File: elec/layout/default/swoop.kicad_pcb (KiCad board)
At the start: 2 copper layers, 100 x 100 mm, 67 parts

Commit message: ios cleanup
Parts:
- added U13: , lib:KEY-SMD_4P-L4.2-W3.2-P2.20-LS4.6, F.Cu at (113.2, 80.2)
- added U14: , lib:KEY-SMD_4P-L4.2-W3.2-P2.20-LS4.6, F.Cu at (121.4, 73.9)
- added U15: , lib:KEY-SMD_4P-L4.2-W3.2-P2.20-LS4.6, F.Cu at (113.2, 73.9)
- added U16: , lib:KEY-SMD_4P-L4.2-W3.2-P2.20-LS4.6, F.Cu at (121.4, 80.2)
- moved C11 10.2 mm to (175.0, 104.6)
- moved C12 10.2 mm to (176.1, 104.6)
- moved C13 10.2 mm to (173.7, 122.8)
- moved C3 10.2 mm to (174.0, 104.6)
- moved C4 10.2 mm to (178.0, 94.8)
- moved C8 10.2 mm to (176.4, 85.6)
- moved C9 10.2 mm to (172.6, 92.4)
- moved R10 10.2 mm to (142.4, 73.6)
- moved R13 10.2 mm to (146.8, 101.0)
- moved R7 10.2 mm to (170.7, 126.1)
- moved U1 10.2 mm to (172.7, 97.6)
- moved U2 10.2 mm to (171.3, 105.8)
- moved U9 10.2 mm to (138.3, 100.8)
- moved C15 10.2 mm to (143.7, 67.9)
- moved C16 10.2 mm to (143.6, 65.8)
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
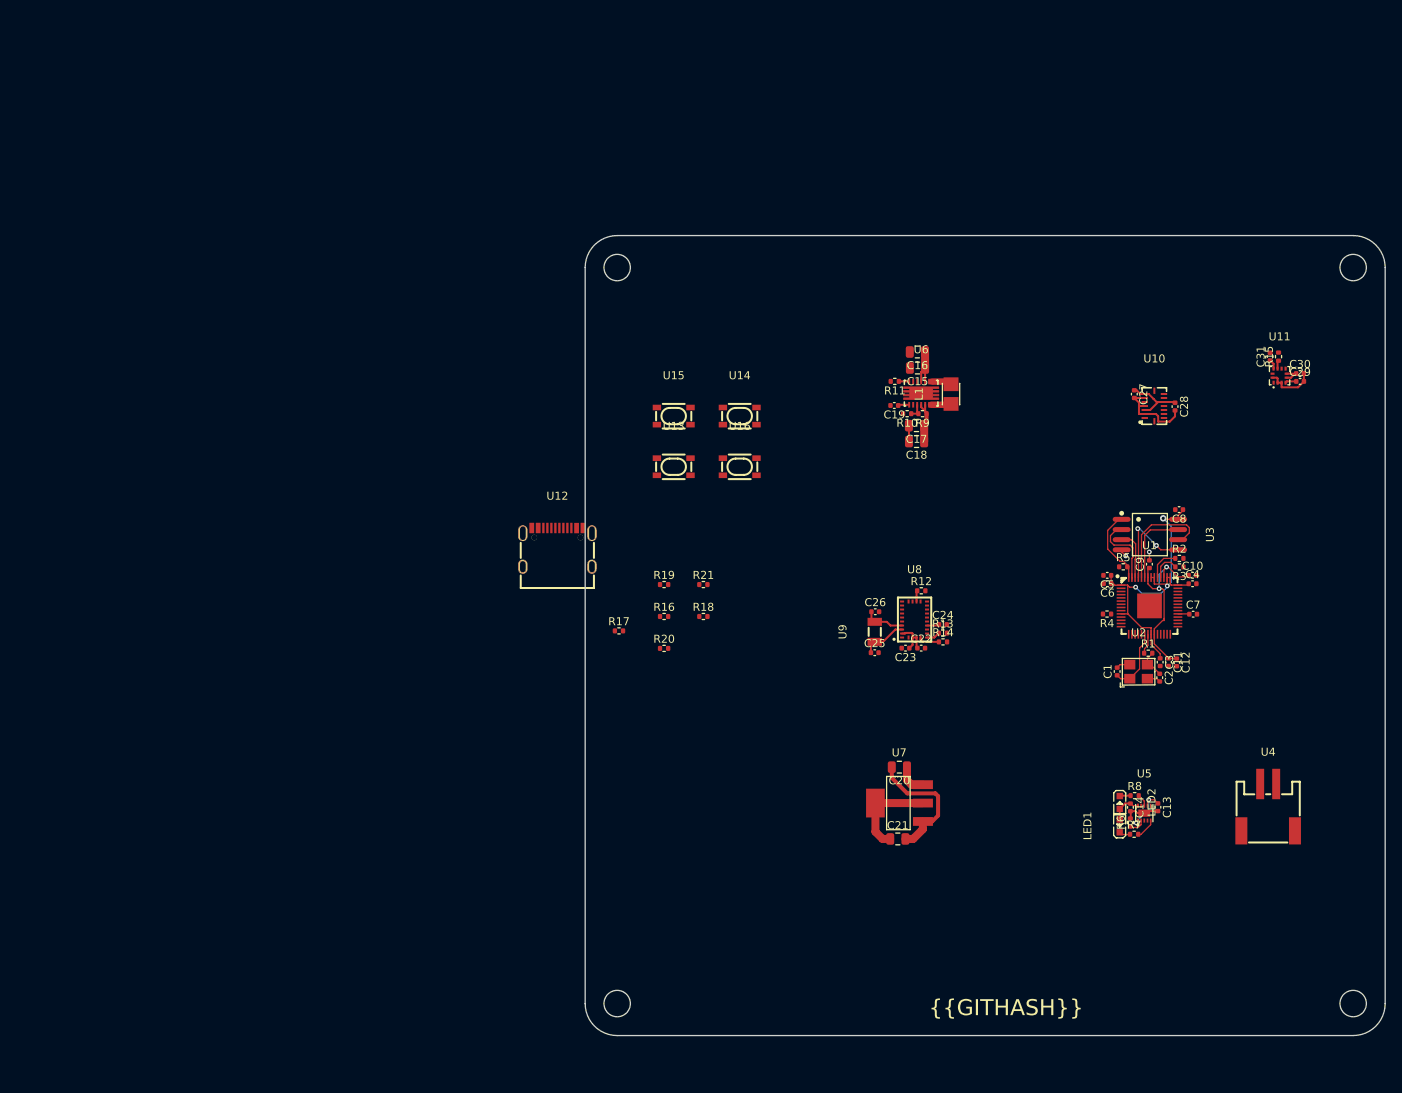
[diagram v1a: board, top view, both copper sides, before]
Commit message: layout 80% complete
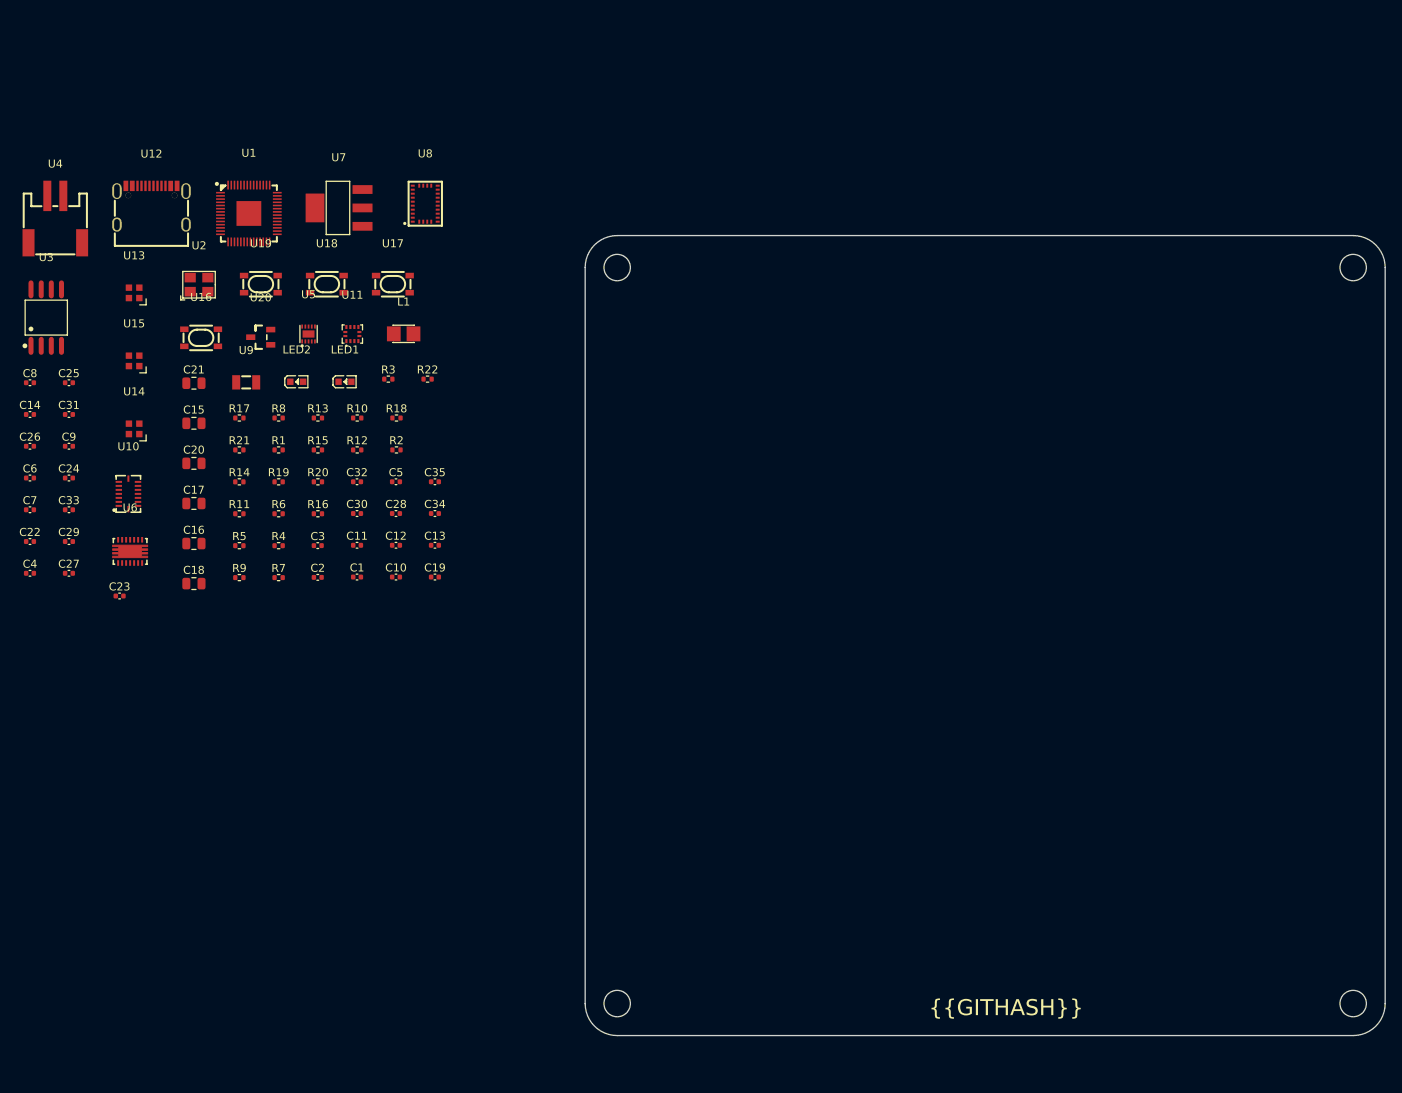
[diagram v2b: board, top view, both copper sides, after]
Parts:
- added C32: 16V 100nF X7R ±10% 0402 Multilayer Ceramic Capacitors MLCC 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, lib:C0402, F.Cu at (73.6, 82.1)
- added C33: 16V 100nF X7R ±10% 0402 Multilayer Ceramic Capacitors MLCC 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, lib:C0402, F.Cu at (37.6, 85.6)
- added C34: 16V 100nF X7R ±10% 0402 Multilayer Ceramic Capacitors MLCC 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, lib:C0402, F.Cu at (83.3, 86.0)
- added C35: 16V 100nF X7R ±10% 0402 Multilayer Ceramic Capacitors MLCC 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, lib:C0402, F.Cu at (83.3, 82.1)
- added R22: 62.5mW Thick Film Resistors ±100ppm/℃ ±1% 1kΩ 0402 Chip Res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, lib:R0402, F.Cu at (82.4, 69.2)
- added U17: , lib:KEY-SMD_4P-L4.2-W3.2-P2.20-LS4.6, F.Cu at (78.1, 57.4)
- added U18: , lib:KEY-SMD_4P-L4.2-W3.2-P2.20-LS4.6, F.Cu at (69.8, 57.4)
- added U19: , lib:KEY-SMD_4P-L4.2-W3.2-P2.20-LS4.6, F.Cu at (61.6, 57.4)
- added U20: , lib:SOT-23-3_L2.9-W1.3-P1.90-LS2.4-BR-CW, F.Cu at (61.6, 64.0)
- C13, C14: value Multilayer Ceramic Capacitors MLCC - SMD/SMT 1uF 6.3V 0402 RoHS -> 25V 1uF X5R ±10% 0402 Multilayer Ceramic Capacitors MLCC - SMD/SMT ROHS
- C15, C16, C17, C18, C20, C21: value Multilayer Ceramic Capacitors MLCC - SMD/SMT 10uF 10V 0805 RoHS -> 25V 10uF X5R ±10% 0805 Multilayer Ceramic Capacitors MLCC - SMD/SMT ROHS
- C19: value Multilayer Ceramic Capacitors MLCC - SMD/SMT 100nF 10V 0402 RoHS -> 16V 100nF X7R ±10% 0402 Multilayer Ceramic Capacitors MLCC - SMD/SMT ROHS
- R10: value Chip Resistor - Surface Mount 180KOhms ±5% 1/16W 0402 RoHS -> 62.5mW Thick Film Resistors ±100ppm/℃ ±1% 180kΩ 0402 Chip Resistor - Surface Mount ROHS
- R11, R9: value Chip Resistor - Surface Mount 1MOhms ±5% 1/16W 0402 RoHS -> 62.5mW Thick Film Resistors ±100ppm/℃ ±1% 1MΩ 0402 Chip Resistor - Surface Mount ROHS
- R7: value Chip Resistor - Surface Mount 120Ohms ±5% 1/16W 0402 RoHS -> 62.5mW Thin Film Resistor ±0.5% ±25ppm/℃ 110Ω 0402 Chip Resistor - Surface Mount ROHS
- R8: value Chip Resistor - Surface Mount 82Ohms ±5% 1/16W 0402 RoHS -> 62.5mW Thick Film Resistors ±100ppm/℃ ±1% 82Ω 0402 Chip Resistor - Surface Mount ROHS
- U13, U14, U15: footprint lib:KEY-SMD_4P-L4.2-W3.2-P2.20-LS4.6 -> lib:LED-SMD_4P-L2.0-W2.0-BR
- moved U4 168.5 mm to (35.9, 49.3)
- moved C29 155.2 mm to (37.6, 89.5)
- moved C31 150.3 mm to (37.6, 73.7), turned to 0 degrees
- moved C14 146.1 mm to (32.7, 73.7), turned to 0 degrees
- moved C7 146.0 mm to (32.7, 85.6)
- moved C4 145.3 mm to (32.7, 93.5)
- moved C8 144.5 mm to (32.7, 69.7), turned to 0 degrees
- moved U3 140.6 mm to (34.8, 61.5), turned to 0 degrees
- moved C9 135.9 mm to (37.6, 77.6), turned to 0 degrees
- moved C6 135.3 mm to (32.7, 81.6), turned to 0 degrees
- moved C27 135.0 mm to (37.6, 93.5), turned to 0 degrees
- moved U10 128.7 mm to (45.0, 83.6)
- moved U2 127.0 mm to (53.9, 57.4)
- moved U1 122.8 mm to (60.1, 48.5)
- moved R15 120.6 mm to (68.7, 78.1), turned to 0 degrees
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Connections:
- net vcc-8 renamed vcc-18
- C10 pad 1: vcc-1 -> vcc-5
- C11 pad 1: vcc-1 -> vcc-5
- C12 pad 1: vcc-1 -> vcc-5
- C13 pad 1: vcc-2 -> vcc-6
- C14 pad 1: vcc-3 -> vcc-7
- C15 pad 1: vcc-3 -> vcc-7
- C16 pad 1: vcc-3 -> vcc-7
- C17 pad 1: vcc-4 -> vcc-10
- C18 pad 1: vcc-4 -> vcc-10
- C20 pad 1: vcc-4 -> vcc-10
- C9 pad 1: vcc-1 -> vcc-5
- LED1 pad 2: vcc-3 -> vcc-7
- LED2 pad 2: vcc-3 -> vcc-7
- R18 pad 1: vcc-5 -> vcc-15
- R18 pad 2: out-2 -> vcc-2
- R19 pad 1: vcc-6 -> vcc-16
- R19 pad 2: out-4 -> vcc-3
- R20 pad 1: vcc-7 -> vcc-17
- R20 pad 2: out-6 -> vcc-4
- R21 pad 2: out-8 -> tx
- R9 pad 1: vcc-4 -> vcc-10
- U1 pad 2: io -> vcc-1
- U1 pad 23: vcc-1 -> vcc-5
- U1 pad 3: gpio1 -> vcc-2
- U1 pad 4: gpio2 -> vcc-3
- U1 pad 45: vcc-1 -> vcc-5
- U1 pad 5: gpio3 -> vcc-4
- U1 pad 50: vcc-1 -> vcc-5
- U11 pad 7: int-1 -> int
- U12 pad A4: vcc-2 -> vcc-6
- U12 pad A6: dp-1 -> dp
- U12 pad A7: dm-1 -> dm
- U12 pad A9: vcc-2 -> vcc-6
- U12 pad B4: vcc-2 -> vcc-6
- U12 pad B6: dp-1 -> dp
- U12 pad B7: dm-1 -> dm
- U12 pad B9: vcc-2 -> vcc-6
- U13 pad 1: out-2 -> vcc
- U13 pad 2: out-2 -> vcc-12
- U13 pad 3: out-3 -> gnd
- U13 pad 4: out-3 -> rx
- U14 pad 1: out-4 -> vcc
- U14 pad 2: out-4 -> vcc-13
- U14 pad 3: out-5 -> gnd
- U14 pad 4: out-5 -> vcc-12
- U15 pad 1: out-6 -> vcc
- U15 pad 2: out-6 -> vcc-14
- U15 pad 3: out-7 -> gnd
- U15 pad 4: out-7 -> vcc-13
- U16 pad 1: out-8 -> vcc-2
- U16 pad 2: out-8 -> vcc-2
- U16 pad 3: out-9 -> gnd
- U16 pad 4: out-9 -> gnd
- U4 pad 2: vcc-3 -> vcc-7
- U5 pad 1: vcc-2 -> vcc-6
- U5 pad 10: vcc-3 -> vcc-7
- U5 pad 7: vcc-2 -> vcc-6
- U6 pad 10: vcc-3 -> vcc-7
- U6 pad 11: vcc-3 -> vcc-7
- U6 pad 4: vcc-4 -> vcc-10
- U6 pad 5: vcc-4 -> vcc-10
- U7 pad 3: vcc-4 -> vcc-10
- U8 pad 14: int -> vcc-1
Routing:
- net vcc: track 71.7 -> 0.00 mm, vias 3 -> 0
- net gnd: track 45.2 -> 0.00 mm, vias 2 -> 0
- net vcc-1: track 23.4 -> 0.00 mm, vias 2 -> 0
- net sck: track 14.4 -> 0.00 mm
- net io0: track 12.8 -> 0.00 mm, vias 2 -> 0
- net vcc-4: track 10.1 -> 0.00 mm
- net vcc-3: track 9.80 -> 0.00 mm
- net io3: track 9.73 -> 0.00 mm
- net io1: track 9.57 -> 0.00 mm
- net cs: track 9.55 -> 0.00 mm
- net xin: track 8.08 -> 0.00 mm
- net io2: track 6.20 -> 0.00 mm
- net vcc-2: track 6.03 -> 0.00 mm, vias 2 -> 0
- net xin32: track 5.61 -> 0.00 mm
- net xout32: track 5.04 -> 0.00 mm
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
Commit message: merging in layouts (#20)
* merging in layouts

* cleaner commit

* remove test container from ci job

* fix missing V in physical

* increase i_q for it to solve

---------

Co-authored-by: Timot05 <timothee.peter@mac.com>
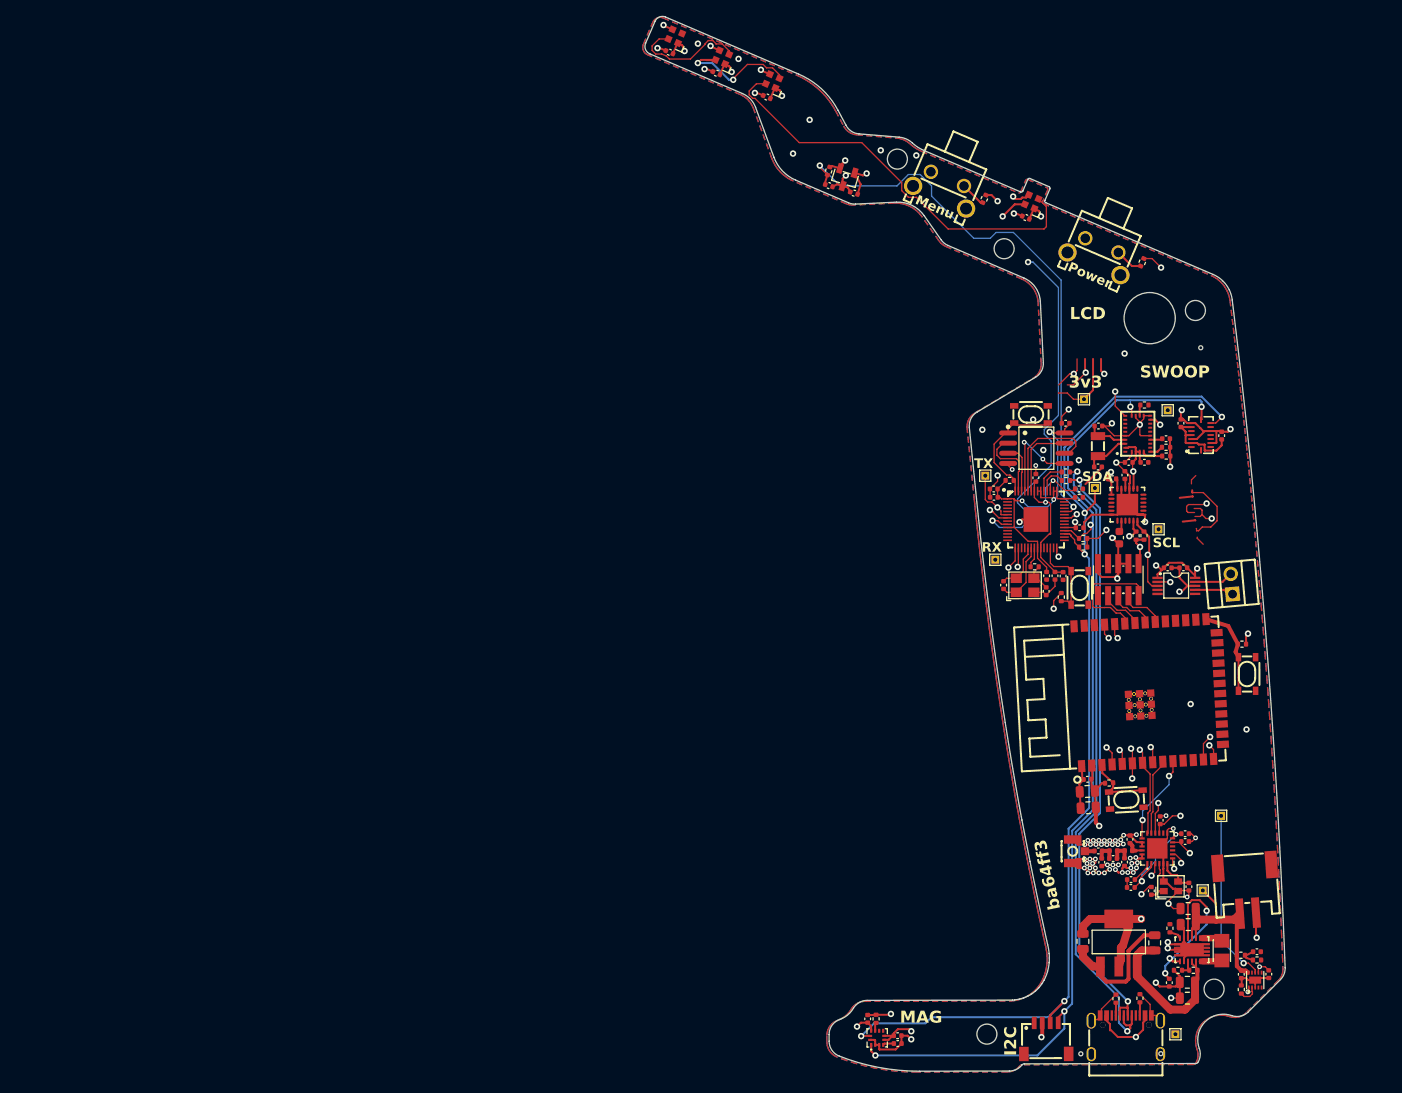
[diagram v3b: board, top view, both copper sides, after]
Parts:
- removed LED1, LED2: , lib:LED0603-RD
- added C36: 25V 10uF X5R ±10% 0805 Multilayer Ceramic Capacitors MLCC -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, lib:C0805, F.Cu at (164.9, 120.8)
- added C37: 25V 10uF X5R ±10% 0805 Multilayer Ceramic Capacitors MLCC -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, lib:C0805, F.Cu at (165.0, 122.8)
- added C38: 50V 12pF C0G ±5% 0402 Multilayer Ceramic Capacitors MLCC - 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, lib:C0402, F.Cu at (172.9, 133.2)
- added C39: 50V 12pF C0G ±5% 0402 Multilayer Ceramic Capacitors MLCC - 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, lib:C0402, F.Cu at (177.6, 132.7)
- added C40: 50V 470nF X5R ±10% 0402 Multilayer Ceramic Capacitors MLCC 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, lib:C0402, F.Cu at (170.3, 132.8)
- added C41: 16V 100nF X7R ±10% 0402 Multilayer Ceramic Capacitors MLCC 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, lib:C0402, F.Cu at (174.0, 124.4)
- added C42: 16V 100nF X7R ±10% 0402 Multilayer Ceramic Capacitors MLCC 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, lib:C0402, F.Cu at (177.1, 127.0)
- added C43: 50V 10nF X7R ±10% 0402 Multilayer Ceramic Capacitors MLCC -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, lib:C0402, F.Cu at (177.1, 126.1)
- added C44: 50V 10nF X7R ±10% 0402 Multilayer Ceramic Capacitors MLCC -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, lib:C0402, F.Cu at (170.3, 131.8)
- added C45: 50V 0.8pF 0402 Multilayer Ceramic Capacitors MLCC - SMD/SMT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, lib:C0402, F.Cu at (170.2, 126.8)
- added C46: 50V 1.2pF C0G 0402 Multilayer Ceramic Capacitors MLCC - SMD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, lib:C0402, F.Cu at (169.5, 129.6)
- added C47: 50V 1.2pF C0G 0402 Multilayer Ceramic Capacitors MLCC - SMD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, lib:C0402, F.Cu at (166.7, 129.6)
- added C48: 50V 0.5pF C0G 0402 Multilayer Ceramic Capacitors MLCC - SMD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, lib:C0402, F.Cu at (168.1, 129.2)
- added C49: 50V 100pF C0G ±5% 0402 Multilayer Ceramic Capacitors MLCC -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, lib:C0402, F.Cu at (166.3, 128.2)
- added C50: 16V 100nF X7R ±10% 0402 Multilayer Ceramic Capacitors MLCC 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, lib:C0402, F.Cu at (157.2, 49.0)
- added C51: 16V 100nF X7R ±10% 0402 Multilayer Ceramic Capacitors MLCC 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, lib:C0402, F.Cu at (124.8, 34.0)
- added C52: 16V 100nF X7R ±10% 0402 Multilayer Ceramic Capacitors MLCC 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, lib:C0402, F.Cu at (118.5, 31.0)
- added C53: 16V 100nF X7R ±10% 0402 Multilayer Ceramic Capacitors MLCC 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, lib:C0402, F.Cu at (112.6, 28.4)
- added C54: 16V 100nF X7R ±10% 0402 Multilayer Ceramic Capacitors MLCC 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, lib:C0402, F.Cu at (135.7, 46.0)
- added C55: 16V 100nF X7R ±10% 0402 Multilayer Ceramic Capacitors MLCC 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, lib:C0402, F.Cu at (132.6, 45.0)
- added C56: 25V 1uF X5R ±10% 0402 Multilayer Ceramic Capacitors MLCC - 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, lib:C0402, F.Cu at (174.9, 92.8)
- added C57: 25V 1uF X5R ±10% 0402 Multilayer Ceramic Capacitors MLCC - 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, lib:C0402, F.Cu at (176.9, 92.8)
- added J1: , lib:CONN-SMD_4P-P1.00_SM04B-SRSS-TB-LF-SN, F.Cu at (159.8, 151.7)
- added L2: , lib:L0402, F.Cu at (170.0, 128.2)
- added L3: , lib:L0402, F.Cu at (168.1, 128.2)
- added R23: 62.5mW Thick Film Resistors 50V ±100ppm/℃ ±1% 4.7kΩ 0402 Ch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, lib:R0402, F.Cu at (168.5, 146.7)
- added R24: 62.5mW Thick Film Resistors 50V ±100ppm/℃ ±1% 4.7kΩ 0402 Ch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, lib:R0402, F.Cu at (171.5, 146.6)
- added R25: 62.5mW Thick Film Resistors 50V ±100ppm/℃ ±1% 10kΩ 0402 Chi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, lib:R0402, F.Cu at (152.0, 46.7)
- added R26: 62.5mW Thick Film Resistors 50V ±100ppm/℃ ±1% 10kΩ 0402 Chi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, lib:R0402, F.Cu at (171.8, 54.6)
- added R27: 62.5mW Thick Film Resistors ±100ppm/℃ ±1% 3.24kΩ 0402 Chip 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, lib:R0402, F.Cu at (132.6, 43.2)
- added U21: , lib:LGA-16_L4.5-W3.0-P0.50-BL, F.Cu at (179.1, 76.2)
- added U22: , lib:QFN-24_L4.0-W4.0-P0.50-BL-EP2.7, F.Cu at (169.9, 84.9)
- added U23: , lib:LGA-12_L2.0-W2.0-P0.50-BL, F.Cu at (138.6, 151.6)
- added U24: , lib:WIRELM-SMD_ESP32-S3-WROOM-1, F.Cu at (172.6, 108.4)
- added U25: , lib:KEY-SMD_4P-L4.2-W3.2-P2.20-LS4.6, F.Cu at (169.8, 121.8)
- added U26: , lib:QFN-24_L4.0-W4.0-P0.50-BL-EP2.6, F.Cu at (173.6, 127.9)
- added U27: , lib:OSC-SMD_4P-L2.0-W1.6-BL, F.Cu at (175.3, 132.6)
- added U28: , lib:IPEX-SMD_BWIPX-1-001E, F.Cu at (163.8, 128.3)
- added U29: , lib:KEY-SMD_4P-L4.2-W3.2-P2.20-LS4.6, F.Cu at (184.9, 106.1)
- added U30: , lib:HDR-SMD_10P-P1.27-V-M-R2-C5-LS5.3, F.Cu at (168.8, 94.3)
- added U31: , lib:USB-C-SMD_KH-TYPE-C-16P, F.Cu at (169.7, 151.2)
- added U32: , lib:LED-SMD_4P-L2.0-W2.0-BR, F.Cu at (157.9, 47.1)
- added U33: , lib:LED-SMD_4P-L2.0-W2.0-BR, F.Cu at (125.6, 32.0)
- added U34: , lib:LED-SMD_4P-L2.0-W2.0-BR, F.Cu at (119.3, 29.0)
- added U35: , lib:LED-SMD_4P-L2.0-W2.0-BR, F.Cu at (113.4, 26.4)
- added U36: , lib:SW-TH_TS-1093C-A7B3-D1, F.Cu at (146.9, 45.4)
- added U37: , lib:SW-TH_TS-1093C-A7B3-D1, F.Cu at (166.2, 53.7)
- added U38: , lib:SOT-23-3_L2.9-W1.3-P0.95-LS2.4-BR, F.Cu at (134.6, 44.1)
- added U39: , lib:VSSOP-10_L3.0-W3.0-P0.50-LS4.9-BL, F.Cu at (176.0, 95.1)
- added U40: , lib:CONN-TH_DB125-2.54-2P-GN, F.Cu at (182.9, 94.8)
- C1, C2: value 50V 20pF C0G ±5% 0402 Multilayer Ceramic Capacitors MLCC - SMD/SMT ROHS -> 50V 18pF C0G ±5% 0402 Multilayer Ceramic Capacitors MLCC - SMD/SMT ROHS
- C23, C30: value 25V 1uF X5R ±10% 0402 Multilayer Ceramic Capacitors MLCC - SMD/SMT ROHS -> 16V 100nF X7R ±10% 0402 Multilayer Ceramic Capacitors MLCC - SMD/SMT ROHS
- C24, C33: value 16V 100nF X7R ±10% 0402 Multilayer Ceramic Capacitors MLCC - SMD/SMT ROHS -> 25V 1uF X5R ±10% 0402 Multilayer Ceramic Capacitors MLCC - SMD/SMT ROHS
- C25: value 50V 22pF C0G ±5% 0402 Multilayer Ceramic Capacitors MLCC - SMD/SMT ROHS -> 16V 100nF X7R ±10% 0402 Multilayer Ceramic Capacitors MLCC - SMD/SMT ROHS
- C26: value 50V 22pF C0G ±5% 0402 Multilayer Ceramic Capacitors MLCC - SMD/SMT ROHS -> 50V 18pF C0G ±5% 0402 Multilayer Ceramic Capacitors MLCC - SMD/SMT ROHS
- C27: value 16V 100nF X7R ±10% 0402 Multilayer Ceramic Capacitors MLCC - SMD/SMT ROHS -> 50V 18pF C0G ±5% 0402 Multilayer Ceramic Capacitors MLCC - SMD/SMT ROHS
- C31: value 16V 100nF X7R ±10% 0402 Multilayer Ceramic Capacitors MLCC - SMD/SMT ROHS -> 50V 2.2nF X7R ±10% 0603 Multilayer Ceramic Capacitors MLCC - SMD/SMT ROHS; footprint lib:C0402 -> lib:C0603
- R1, R15, R22: value 62.5mW Thick Film Resistors ±100ppm/℃ ±1% 1kΩ 0402 Chip Resistor - Surface Mount ROHS -> 62.5mW Thick Film Resistors 50V ±100ppm/℃ ±1% 10kΩ 0402 Chip Resistor - Surface Mount ROHS
- R10: value 62.5mW Thick Film Resistors ±100ppm/℃ ±1% 180kΩ 0402 Chip Resistor - Surface Mount ROHS -> 62.5mW Thick Film Resistors 50V ±1% ±200ppm/℃ 105kΩ 0402 Chip Resistor - Surface Mount ROHS
- R11: value 62.5mW Thick Film Resistors ±100ppm/℃ ±1% 1MΩ 0402 Chip Resistor - Surface Mount ROHS -> 62.5mW Thick Film Resistors 50V ±100ppm/℃ ±1% 1MΩ 0402 Chip Resistor - Surface Mount ROHS
- R12: value 62.5mW Thick Film Resistors ±100ppm/℃ ±1% 10kΩ 0402 Chip Resistor - Surface Mount ROHS -> 62.5mW Thick Film Resistors 50V ±100ppm/℃ ±1% 16.2kΩ 0402 Chip Resistor - Surface Mount ROHS
- R13: value 62.5mW Thick Film Resistors ±100ppm/℃ ±1% 10kΩ 0402 Chip Resistor - Surface Mount ROHS -> 62.5mW Thick Film Resistors 50V ±100ppm/℃ ±1% 17.8kΩ 0402 Chip Resistor - Surface Mount ROHS
- R14, R18, R19, R21: value 62.5mW Thick Film Resistors ±100ppm/℃ ±1% 10kΩ 0402 Chip Resistor - Surface Mount ROHS -> 62.5mW Thick Film Resistors 50V ±100ppm/℃ ±1% 10kΩ 0402 Chip Resistor - Surface Mount ROHS
- R16, R17: value 62.5mW Thick Film Resistors ±100ppm/℃ ±1% 5.1kΩ 0402 Chip Resistor - Surface Mount ROHS -> 62.5mW Thick Film Resistors 50V ±100ppm/℃ ±1% 10kΩ 0402 Chip Resistor - Surface Mount ROHS
- R2: value 62.5mW Thick Film Resistors ±100ppm/℃ ±1% 27kΩ 0402 Chip Resistor - Surface Mount ROHS -> 62.5mW Thick Film Resistors 50V ±100ppm/℃ ±1% 10kΩ 0402 Chip Resistor - Surface Mount ROHS
- R20: value 62.5mW Thick Film Resistors ±100ppm/℃ ±1% 10kΩ 0402 Chip Resistor - Surface Mount ROHS -> 62.5mW Thick Film Resistors 50V ±100ppm/℃ ±1% 1kΩ 0402 Chip Resistor - Surface Mount ROHS
- R3: value 62.5mW Thick Film Resistors ±100ppm/℃ ±1% 27kΩ 0402 Chip Resistor - Surface Mount ROHS -> 62.5mW Thick Film Resistors 50V ±100ppm/℃ ±1% 1kΩ 0402 Chip Resistor - Surface Mount ROHS
- R4, R5: value 62.5mW Thick Film Resistors ±100ppm/℃ ±1% 10kΩ 0402 Chip Resistor - Surface Mount ROHS -> 62.5mW Thick Film Resistors 50V ±100ppm/℃ ±1% 27Ω 0402 Chip Resistor - Surface Mount ROHS
- R6: value 62.5mW Thick Film Resistors ±100ppm/℃ ±1% 510Ω 0402 Chip Resistor - Surface Mount ROHS -> 62.5mW Thick Film Resistors 50V ±100ppm/℃ ±1% 2kΩ 0402 Chip Resistor - Surface Mount ROHS
- R7: value 62.5mW Thin Film Resistor ±0.5% ±25ppm/℃ 110Ω 0402 Chip Resistor - Surface Mount ROHS -> 62.5mW Thick Film Resistors 50V ±100ppm/℃ ±1% 2kΩ 0402 Chip Resistor - Surface Mount ROHS
- R8: value 62.5mW Thick Film Resistors ±100ppm/℃ ±1% 82Ω 0402 Chip Resistor - Surface Mount ROHS -> 100mW Thick Film Resistors ±100ppm/℃ ±1% 1.07kΩ 0402 Chip Resistor - Surface Mount ROHS
- R9: value 62.5mW Thick Film Resistors ±100ppm/℃ ±1% 1MΩ 0402 Chip Resistor - Surface Mount ROHS -> 62.5mW Thick Film Resistors 50V ±100ppm/℃ ±1% 698kΩ 0402 Chip Resistor - Surface Mount ROHS
- U10: footprint lib:LGA-16_L4.5-W3.0-P0.50-BL -> TestPoint:TestPoint_THTPad_1.0x1.0mm_Drill0.5mm
- U11: footprint lib:LGA-12_L2.0-W2.0-P0.50-BL -> lib:CONN-SMD_P2.00_S2B-PH-SM4-TB-LF-SN
- U12: footprint lib:USB-C-SMD_KH-TYPE-C-16P -> lib:WSON-10_L2.0-W2.0-P0.40-BL-EP
- U13: footprint lib:LED-SMD_4P-L2.0-W2.0-BR -> lib:VSON-14_L4.0-W3.0-P0.50-BL-EP_TI_DSJ
- U14: footprint lib:LED-SMD_4P-L2.0-W2.0-BR -> lib:SOT-223-3_L6.5-W3.4-P2.30-LS7.0-BR
- U15: footprint lib:LED-SMD_4P-L2.0-W2.0-BR -> TestPoint:TestPoint_THTPad_1.0x1.0mm_Drill0.5mm
- U16, U17, U18: footprint lib:KEY-SMD_4P-L4.2-W3.2-P2.20-LS4.6 -> TestPoint:TestPoint_THTPad_1.0x1.0mm_Drill0.5mm
- U19: footprint lib:KEY-SMD_4P-L4.2-W3.2-P2.20-LS4.6 -> lib:LGA-28_L5.2-W3.8-P0.50-BL
- U2: footprint lib:OSC-SMD_4P-L3.2-W2.5-BL -> lib:KEY-SMD_4P-L4.2-W3.2-P2.20-LS4.6
- U20: footprint lib:SOT-23-3_L2.9-W1.3-P1.90-LS2.4-BR-CW -> lib:FC-135R_L3.2-W1.5
- U3: footprint lib:SOIC-8_L5.3-W5.3-P1.27-LS8.0-BL -> lib:KEY-SMD_4P-L4.2-W3.2-P2.20-LS4.6
- U4: footprint lib:CONN-SMD_P2.00_S2B-PH-SM4-TB-LF-SN -> lib:OSC-SMD_4P-L3.2-W2.5-BL
- U5: footprint lib:WSON-10_L2.0-W2.0-P0.40-BL-EP -> lib:SOIC-8_L5.3-W5.3-P1.27-LS8.0-BL
- U6: footprint lib:VSON-14_L4.0-W3.0-P0.50-BL-EP_TI_DSJ -> TestPoint:TestPoint_THTPad_1.0x1.0mm_Drill0.5mm
- U7: footprint lib:SOT-223-3_L6.5-W3.4-P2.30-LS7.0-BR -> TestPoint:TestPoint_THTPad_1.0x1.0mm_Drill0.5mm
- U8: footprint lib:LGA-28_L5.2-W3.8-P0.50-BL -> TestPoint:TestPoint_THTPad_1.0x1.0mm_Drill0.5mm
- U9: footprint lib:FC-135R_L3.2-W1.5 -> TestPoint:TestPoint_THTPad_1.0x1.0mm_Drill0.5mm
- moved U12 168.6 mm to (185.9, 144.4), turned to 0.1 degrees
- moved C14 166.8 mm to (184.1, 143.6), turned to -89.9 degrees
- moved C22 161.7 mm to (186.1, 140.8), turned to 0.1 degrees
- moved U13 155.7 mm to (178.0, 140.6), turned to 0.1 degrees
- moved U15 155.0 mm to (175.9, 151.1)
- moved C29 144.7 mm to (181.7, 76.3), turned to -89.9 degrees
- moved R8 139.9 mm to (184.1, 145.5), turned to 90.1 degrees
- moved C15 139.2 mm to (177.5, 137.4), turned to -179.9 degrees
- moved U14 138.8 mm to (168.8, 139.7), turned to -89.9 degrees
- moved C17 137.9 mm to (177.4, 144.6), turned to -179.9 degrees
- moved C25 137.3 mm to (174.7, 76.7), turned to 0.1 degrees
- moved R13 135.5 mm to (186.1, 141.9), turned to 0.1 degrees
- moved C18 134.6 mm to (177.4, 146.6), turned to -179.9 degrees
- moved C20 134.2 mm to (173.3, 139.7), turned to 90.1 degrees
- moved C26 133.5 mm to (166.2, 80.2), turned to 0.1 degrees
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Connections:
- net gpio9 renamed micro.micro-cs
- net miso renamed micro.micro-miso
- net sck-1 renamed micro.micro-sck
- net vcc-5 renamed micro.micro.micro-vcc
- C13 pad 1: vcc-6 -> power_supply-vcc
- C14 pad 1: vcc-7 -> power_supply.battery-vcc
- C15 pad 1: vcc-7 -> power_supply.battery-vcc
- C16 pad 1: vcc-7 -> power_supply.battery-vcc
- C17 pad 1: vcc-10 -> power_supply.buckboost-vcc
- C18 pad 1: vcc-10 -> power_supply.buckboost-vcc
- C2 pad 1: out -> micro.micro.osc.osc-out
- C20 pad 1: vcc-10 -> power_supply.buckboost-vcc
- C22 pad 1: vcc -> power_supply.battery_voltage_sensor-out
- C24 pad 1: cap -> vcc
- C25 pad 1: xin32 -> cap
- C26 pad 1: xout32 -> xin32
- C27 pad 1: vcc -> xout32
- C29 pad 1: c1 -> vcc
- C30 pad 1: vcc -> gnd
- C30 pad 2: gnd -> regout
- C31 pad 1: vcc -> gnd
- C31 pad 2: gnd -> cpout
- C32 pad 1: vcc -> c1
- R1 pad 1: xout -> vcc
- R1 pad 2: out -> run
- R10 pad 1: out-1 -> power_supply.buckboost.tps_buck_boost.feedback_div-out
- R11 pad 1: pg -> power_supply.buckboost.tps_buck_boost.ic-pg
- R12 pad 1: com3 -> power_supply.battery-vcc
- R12 pad 2: gnd -> power_supply.battery_voltage_sensor-out
- R13 pad 1: ps0 -> power_supply.battery_voltage_sensor-out
- R14 pad 1: ps1 -> com3
- R15 pad 1: miso-1 -> ps0
- R16 pad 1: cc1 -> ps1
- R17 pad 1: cc2 -> interrupt
- R17 pad 2: gnd -> vcc
- R18 pad 1: vcc-15 -> sda
- R18 pad 2: vcc-2 -> vcc
- R19 pad 1: vcc-16 -> scl
- R19 pad 2: vcc-3 -> vcc
- R2 pad 1: usb_dp -> vcc
- R2 pad 2: dp -> micro.micro-cs-1
- R20 pad 1: vcc-17 -> imu.lis3mdltr.ic-miso
- R20 pad 2: vcc-4 -> gnd
- R21 pad 1: vcc-18 -> vcc
- R21 pad 2: tx -> radio._micro.ic-en
- R22 pad 2: vcc-11 -> radio._micro.ic-io0
- R3 pad 1: dm -> xout
- R3 pad 2: usb_dm -> micro.micro.osc.osc-out
- R4 pad 1: vcc -> usb_dp
- R4 pad 2: run -> dp
- R5 pad 1: vcc -> dm
- R5 pad 2: cs -> usb_dm
- R6 pad 1: iset -> sda
- R6 pad 2: gnd -> vcc
- R7 pad 1: cathode -> scl
- R7 pad 2: gnd-5 -> vcc
- R8 pad 1: cathode-1 -> iset
- R8 pad 2: gnd-6 -> gnd
- R9 pad 1: vcc-10 -> power_supply.buckboost-vcc
- R9 pad 2: out-1 -> power_supply.buckboost.tps_buck_boost.feedback_div-out
- U1 pad 15: gpio12 -> micro-vcc-1
- U1 pad 16: gpio13 -> micro-vcc-2
- U1 pad 2: vcc-1 -> gpio0
- U1 pad 28: gpio17 -> micro-vcc-5
- U1 pad 3: vcc-2 -> gpio1
- U1 pad 36: gpio24 -> micro-vcc
- U1 pad 38: gpio26_a0 -> micro-vcc-4
- U1 pad 4: vcc-3 -> gpio2
- U1 pad 5: vcc-4 -> gpio3
- U1 pad 51: io3 -> micro.micro-io3
- U1 pad 52: sck -> micro.micro-sck-1
- U1 pad 53: io0 -> micro.micro-io0
- U1 pad 54: io2 -> micro.micro-io2
- U1 pad 55: io1 -> micro.micro-io1
- U1 pad 56: cs -> micro.micro-cs-1
- U1 pad 9: gpio7 -> micro-vcc-3
- U10 pad 1: int2 -> micro-vcc
- U11 pad 1: scl -> gnd
- U11 pad 2: gnd -> power_supply.battery-vcc
- U11 pad 3: gnd -> (no net)
- U11 pad 4: c1 -> (no net)
- U12 pad 1: gnd -> power_supply-vcc
- U12 pad 2: gnd -> iset
- U12 pad 4: gnd -> preterm
- U13 pad 1: vcc -> vina
- U13 pad 2: vcc-12 -> gnd
- U13 pad 3: gnd -> power_supply.buckboost.tps_buck_boost.feedback_div-out
- U13 pad 4: rx -> power_supply.buckboost-vcc
- U14 pad 1: vcc -> gnd
- U14 pad 2: vcc-13 -> vcc
- U14 pad 3: gnd -> power_supply.buckboost-vcc
- U14 pad 4: vcc-12 -> vcc
- U15 pad 1: vcc -> power_supply-vcc
- U16 pad 1: vcc-2 -> vcc
- U17 pad 1: vcc-3 -> power_supply.battery-vcc
- U18 pad 1: vcc-4 -> micro-vcc-5
- U19 pad 1: tx -> pin1
- U19 pad 2: tx -> gnd
- U19 pad 3: gnd -> vcc
- U19 pad 4: gnd -> vcc
- U2 pad 1: xin -> run
- U2 pad 2: gnd -> run
- U2 pad 3: out -> gnd
- U20 pad 1: vcc -> xin32
- U20 pad 2: gnd -> xout32
- U3 pad 1: cs -> micro.micro-cs-1
- U3 pad 2: io1 -> micro.micro-cs-1
- U3 pad 3: io2 -> gnd
- U4 pad 1: gnd -> xin
- U4 pad 2: vcc-7 -> gnd
- U4 pad 3: (no net) -> micro.micro.osc.osc-out
- U4 pad 4: (no net) -> gnd
- U5 pad 1: vcc-6 -> micro.micro-cs-1
- U5 pad 2: iset -> micro.micro-io1
- U5 pad 3: gnd -> micro.micro-io2
- U5 pad 4: preterm -> gnd
- U5 pad 5: gnd-5 -> micro.micro-io0
- U5 pad 6: nc -> micro.micro-sck-1
- U5 pad 7: vcc-6 -> micro.micro-io3
- U5 pad 8: gnd-6 -> vcc
- U6 pad 1: vina -> scl
- U7 pad 1: gnd -> sda
- U8 pad 1: pin1 -> tx
- U9 pad 1: xin32 -> rx
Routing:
- net gnd: track 0.00 -> 245.1 mm, vias 0 -> 92
- net vcc: track 0.00 -> 163.2 mm, vias 0 -> 28
- net sda: track 0.00 -> 158.5 mm, vias 0 -> 7
- net scl: track 0.00 -> 154.6 mm, vias 0 -> 7
- net dp: track 0.00 -> 80.4 mm, vias 0 -> 2
- net io6: track 0.00 -> 76.7 mm, vias 0 -> 4
- net dm: track 0.00 -> 74.8 mm, vias 0 -> 2
- net micro-vcc-4: track 0.00 -> 72.0 mm, vias 0 -> 2
- net io7: track 0.00 -> 69.8 mm, vias 0 -> 2
- net micro-vcc-5: track 0.00 -> 63.7 mm, vias 0 -> 2
- net micro-vcc-1: track 0.00 -> 61.3 mm, vias 0 -> 1
- net micro-vcc-3: track 0.00 -> 55.0 mm, vias 0 -> 3
- net micro-vcc-2: track 0.00 -> 53.9 mm, vias 0 -> 1
- net ios.led1.ic-vcc: track 0.00 -> 51.6 mm
- net io20: track 0.00 -> 37.4 mm, vias 0 -> 2
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- added copper zone on F.Cu, net gnd
- added copper zone on In1.Cu, net gnd
- added copper zone on B.Cu, net vcc
- added copper zone on In2.Cu, net vcc
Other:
- board size 100 x 100 mm -> 80 x 131.9 mm
- copper layers 2 -> 4
- board text added: "3v3"
- board text added: "I2C"
- board text added: "LCD"
- board text added: "MAG"
- board text added: "Menu"
- board text added: "Power"
- board text added: "RX"
- board text added: "SCL"
- board text added: "SDA"
- board text added: "SWOOP"
- board text added: "TX"
- board text added: "ba64ff3"
- board text removed: "{{GITHASH}}"
